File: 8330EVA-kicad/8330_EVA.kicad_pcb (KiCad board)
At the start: 2 copper layers, 70 parts, among them J1 USB_B_Micro, J2 Conn_Coaxial, J3 Conn_01x03_Male, J4 Conn_Coaxial, J5 Conn_Coaxial, J6 Conn_01x03_Male, T1 T1-1T-KK81, T2 T1-1T-KK81, U1 AMS1117-3.3, U2 FT232H, U3 AD8330, U4 AD8131, U5 AD5312, U6 REF192, Y1 12Mhz

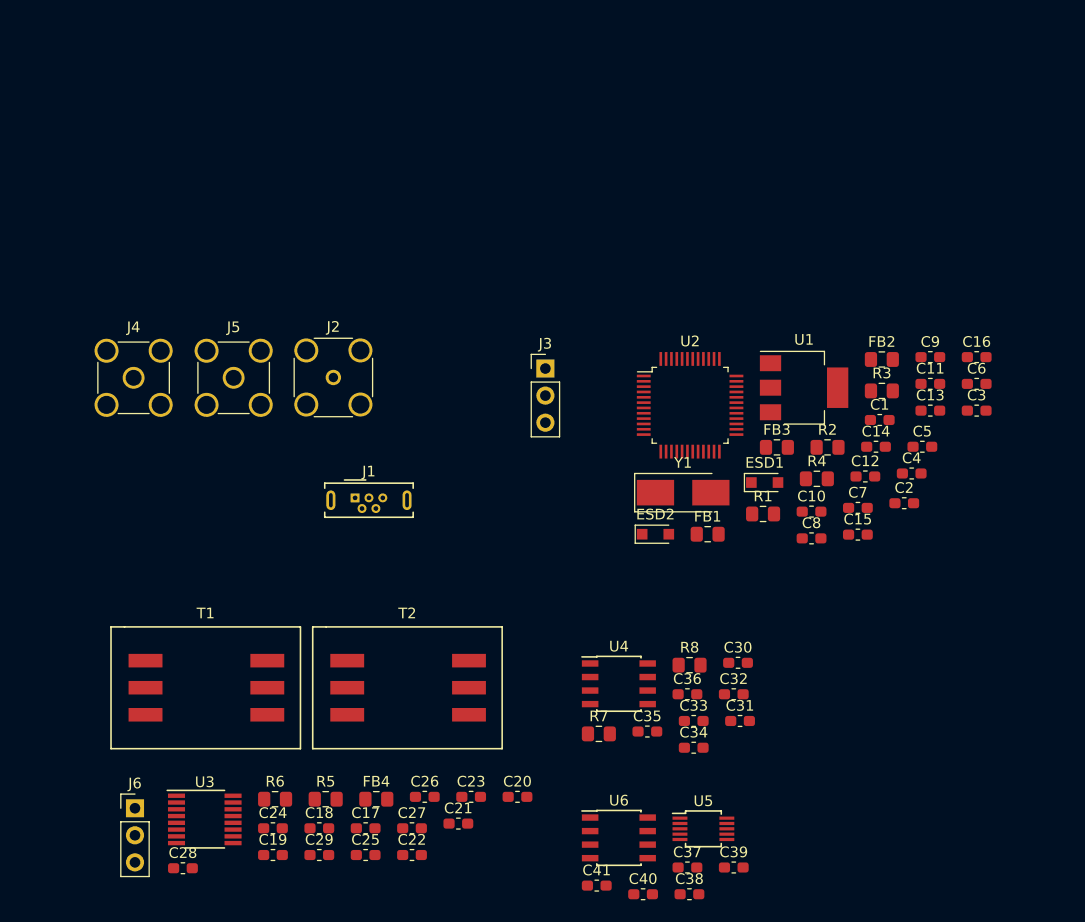
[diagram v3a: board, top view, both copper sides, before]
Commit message: Finished PCB layout, connect Earth to Ground
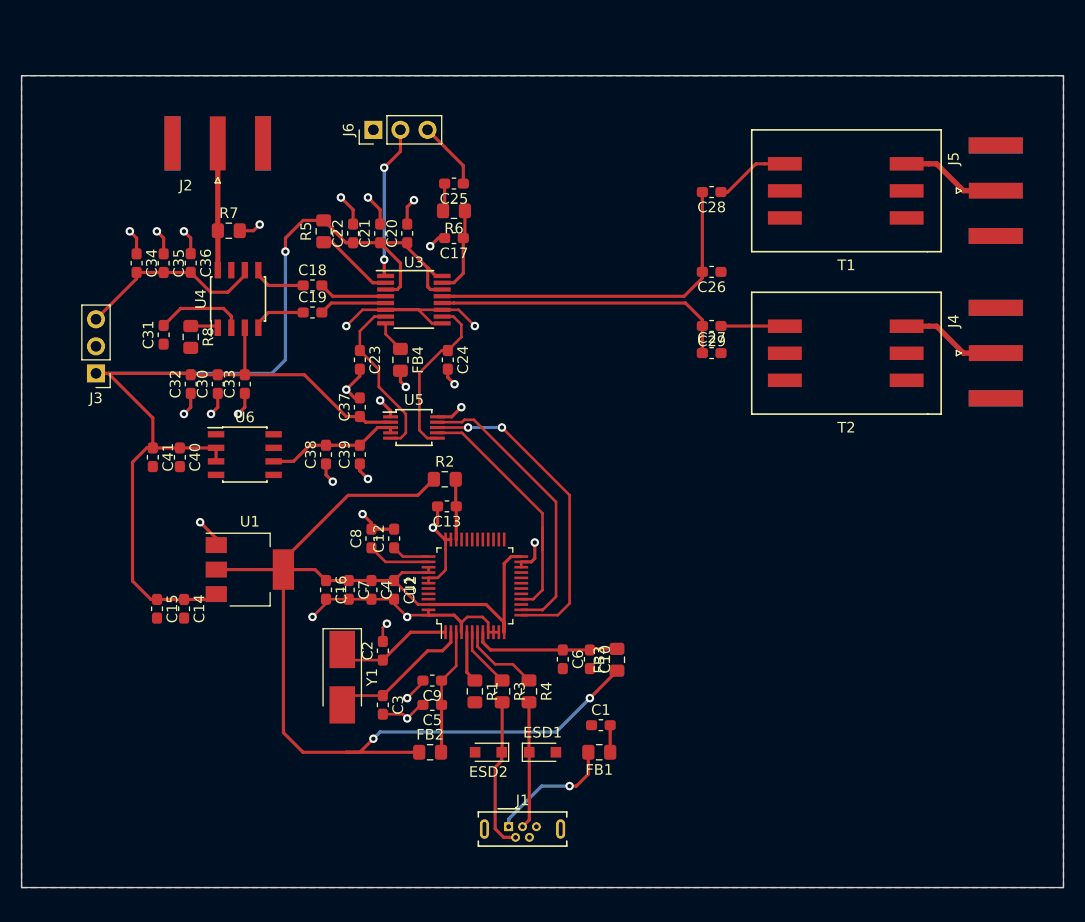
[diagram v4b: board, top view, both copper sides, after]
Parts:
- J2: footprint Connector_Coaxial:SMA_Amphenol_132134-14_Vertical -> Connector_Coaxial:SMA_Amphenol_132289_EdgeMount
- J4, J5: footprint Connector_Coaxial:SMA_Amphenol_132134-11_Vertical -> Connector_Coaxial:SMA_Amphenol_132289_EdgeMount
- moved J4 81.0 mm to (198.1, 79.4)
- moved C28 80.6 mm to (171.4, 64.3), turned to 180 degrees
- moved T1 77.0 mm to (184.2, 63.5), turned to 180 degrees
- moved J5 73.7 mm to (198.1, 64.1)
- moved C34 69.3 mm to (117.5, 70.9), turned to 270 degrees
- moved J6 67.5 mm to (139.7, 58.4), turned to 90 degrees
- moved C14 66.7 mm to (121.9, 103.4), turned to 270 degrees
- moved C15 66.1 mm to (119.4, 103.4), turned to 270 degrees
- moved C31 65.1 mm to (120.0, 77.7), turned to 90 degrees
- moved C16 64.9 mm to (135.3, 101.6), turned to 270 degrees
- moved C25 63.6 mm to (147.3, 63.5), turned to 180 degrees
- moved C35 63.2 mm to (120.0, 70.9), turned to 270 degrees
- moved C3 62.2 mm to (140.6, 112.4), turned to 270 degrees
- moved C29 61.8 mm to (171.4, 76.8), turned to 180 degrees
- moved C36 61.7 mm to (122.6, 70.9), turned to 270 degrees
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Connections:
- C1 pad 1: /USB2SPI/Ground -> Earth
- C10 pad 2: /USB2SPI/Ground -> Earth
- C11 pad 2: /USB2SPI/Ground -> Earth
- C12 pad 2: /USB2SPI/Ground -> Earth
- C13 pad 2: /USB2SPI/Ground -> Earth
- C14 pad 2: /USB2SPI/Ground -> Earth
- C15 pad 2: /USB2SPI/Ground -> Earth
- C16 pad 2: /USB2SPI/Ground -> Earth
- C2 pad 2: /USB2SPI/Ground -> Earth
- C3 pad 2: /USB2SPI/Ground -> Earth
- C4 pad 2: /USB2SPI/Ground -> Earth
- C5 pad 2: /USB2SPI/Ground -> Earth
- C6 pad 2: /USB2SPI/Ground -> Earth
- C7 pad 2: /USB2SPI/Ground -> Earth
- C8 pad 2: /USB2SPI/Ground -> Earth
- C9 pad 2: /USB2SPI/Ground -> Earth
- ESD1 pad 2: /USB2SPI/Ground -> Earth
- ESD2 pad 2: /USB2SPI/Ground -> Earth
- J1 pad 5: /USB2SPI/Ground -> Earth
- J1 pad 6: /USB2SPI/Ground -> Earth
- R1 pad 2: /USB2SPI/Ground -> Earth
- U1 pad 1: /USB2SPI/Ground -> Earth
- U2 pad 10: /USB2SPI/Ground -> Earth
- U2 pad 11: /USB2SPI/Ground -> Earth
- U2 pad 22: /USB2SPI/Ground -> Earth
- U2 pad 23: /USB2SPI/Ground -> Earth
- U2 pad 35: /USB2SPI/Ground -> Earth
- U2 pad 36: /USB2SPI/Ground -> Earth
- U2 pad 4: /USB2SPI/Ground -> Earth
- U2 pad 41: /USB2SPI/Ground -> Earth
- U2 pad 42: /USB2SPI/Ground -> Earth
- U2 pad 47: /USB2SPI/Ground -> Earth
- U2 pad 48: /USB2SPI/Ground -> Earth
- U2 pad 9: /USB2SPI/Ground -> Earth
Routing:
- net /DAC/VCC_+5V: track 0.00 -> 131.1 mm, vias 0 -> 1
- net /USB2SPI/VCCIO: track 0.00 -> 117.9 mm, vias 0 -> 2
- net Earth: track 0.00 -> 112.3 mm, vias 0 -> 29
- net Net-(C26-Pad2): track 0.00 -> 33.2 mm
- net /USB2SPI/MPSSE_SCK: track 0.00 -> 29.9 mm, vias 0 -> 2
- net Net-(C27-Pad1): track 0.00 -> 28.2 mm
- net /USB2SPI/MPSSE_MOSI: track 0.00 -> 27.1 mm
- net /USB2SPI/MPSSE_CS: track 0.00 -> 24.6 mm
- net /VCA/VEE_-5V: track 0.00 -> 18.0 mm
- net /DAC/ChannelB: track 0.00 -> 16.0 mm
- net /DAC/ChannelA: track 0.00 -> 16.0 mm
- net Net-(J6-Pad2): track 0.00 -> 14.4 mm, vias 0 -> 2
- net /USB2SPI/USB_D-: track 0.00 -> 14.4 mm
- net /USB2SPI/VPLL: track 0.00 -> 13.9 mm
- net Net-(C3-Pad1): track 0.00 -> 13.6 mm
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- added copper zone on B.Cu, net Earth
- added copper zone on F.Cu, net Earth
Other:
- board outline added: 97.8 x 76.2 mm

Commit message: 简单修改
1. 修改了差分输出处的布线，提高对称性
2. 修改了USB接口的封装。现在使用完全表面贴装的Mini USB接口
3. 在电路板上添加了要求的信息
4. 生成了BOM表和Gerber文件
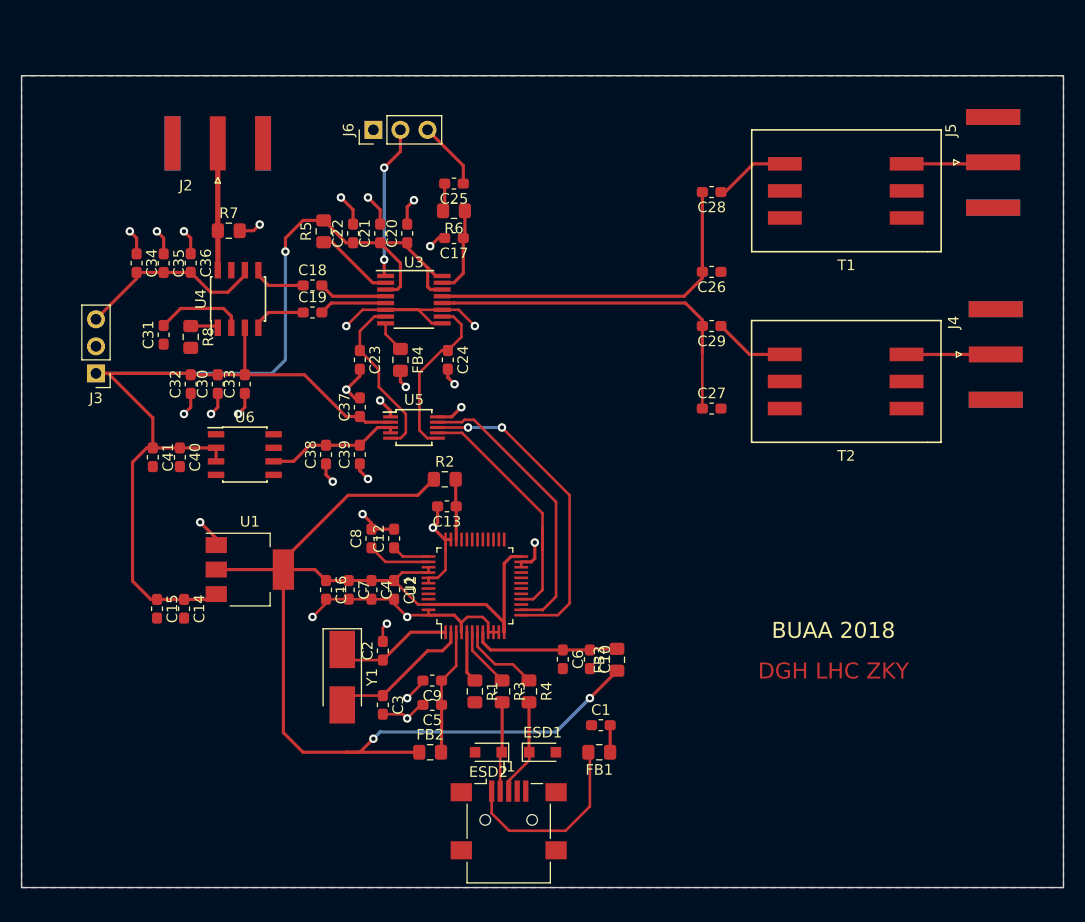
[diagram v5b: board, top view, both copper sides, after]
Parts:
- J1: footprint Connector_USB:USB_Micro-B_Wuerth_614105150721_Vertical -> Connector_USB:USB_Mini-B_Lumberg_2486_01_Horizontal
- moved C27 5.21 mm to (171.4, 84.6)
- moved J5 2.68 mm to (197.9, 61.5)
- moved T2 2.65 mm to (184.1, 81.4)
- moved J1 0.64 mm to (152.4, 123.2)
- moved J4 0.13 mm to (198.1, 79.5)
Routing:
- net /USB2SPI/VBUS: track 12.0 -> 17.7 mm, vias 1 -> 0
- net /USB2SPI/USB_D-: track 14.4 -> 8.70 mm
- net Net-(C27-Pad1): track 28.2 -> 33.4 mm
- net /USB2SPI/USB_D+: track 11.9 -> 9.79 mm
- net /VCA/OPLO: track 9.41 -> 8.13 mm
- net /VCA/OPHI: track 9.41 -> 8.34 mm
- net Net-(C29-Pad1): track 6.00 -> 6.89 mm
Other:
- board text added: "BUAA 2018"
- board text added: "DGH LHC ZKY"

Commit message: 添加M3安装孔，调整SMA焊盘位置
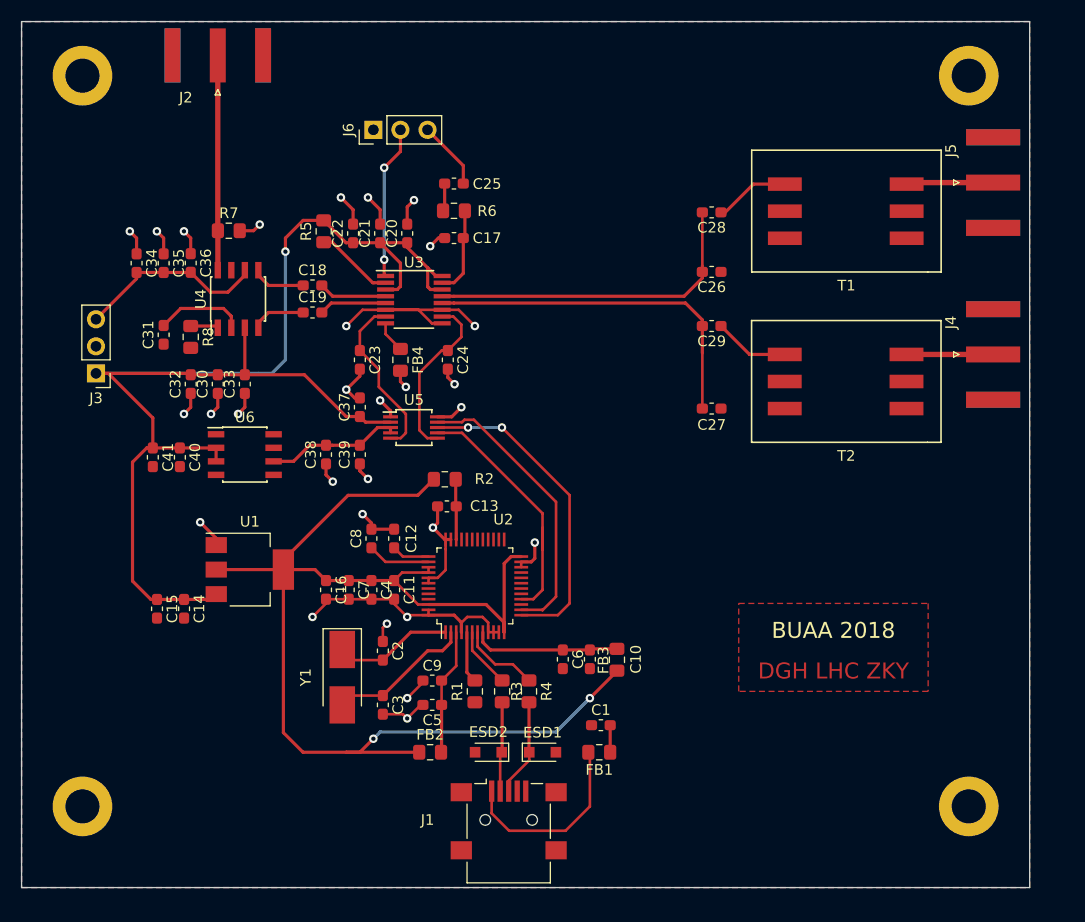
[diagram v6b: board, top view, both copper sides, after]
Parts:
- added REF**: MountingHole_3.2mm_M3_DIN965_Pad, MountingHole:MountingHole_3.2mm_M3_DIN965_Pad, F.Cu at (112.4, 53.3)
- added REF**: MountingHole_3.2mm_M3_DIN965_Pad, MountingHole:MountingHole_3.2mm_M3_DIN965_Pad, F.Cu at (112.4, 121.9)
- added REF**: MountingHole_3.2mm_M3_DIN965_Pad, MountingHole:MountingHole_3.2mm_M3_DIN965_Pad, F.Cu at (195.6, 53.3)
- added REF**: MountingHole_3.2mm_M3_DIN965_Pad, MountingHole:MountingHole_3.2mm_M3_DIN965_Pad, F.Cu at (195.6, 121.9)
- moved J2 8.25 mm to (125.1, 51.4)
- moved C28 1.91 mm to (171.4, 66.2)
- moved T1 1.91 mm to (184.2, 65.4)
- moved J5 1.90 mm to (197.9, 63.4)
- moved J4 0.25 mm to (197.9, 79.5)
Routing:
- net /VCA/SignalIN: track 11.9 -> 20.2 mm
- net Net-(C26-Pad2): track 33.2 -> 31.9 mm
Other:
- board size 97.8 x 76.2 mm -> 94.6 x 81.3 mm

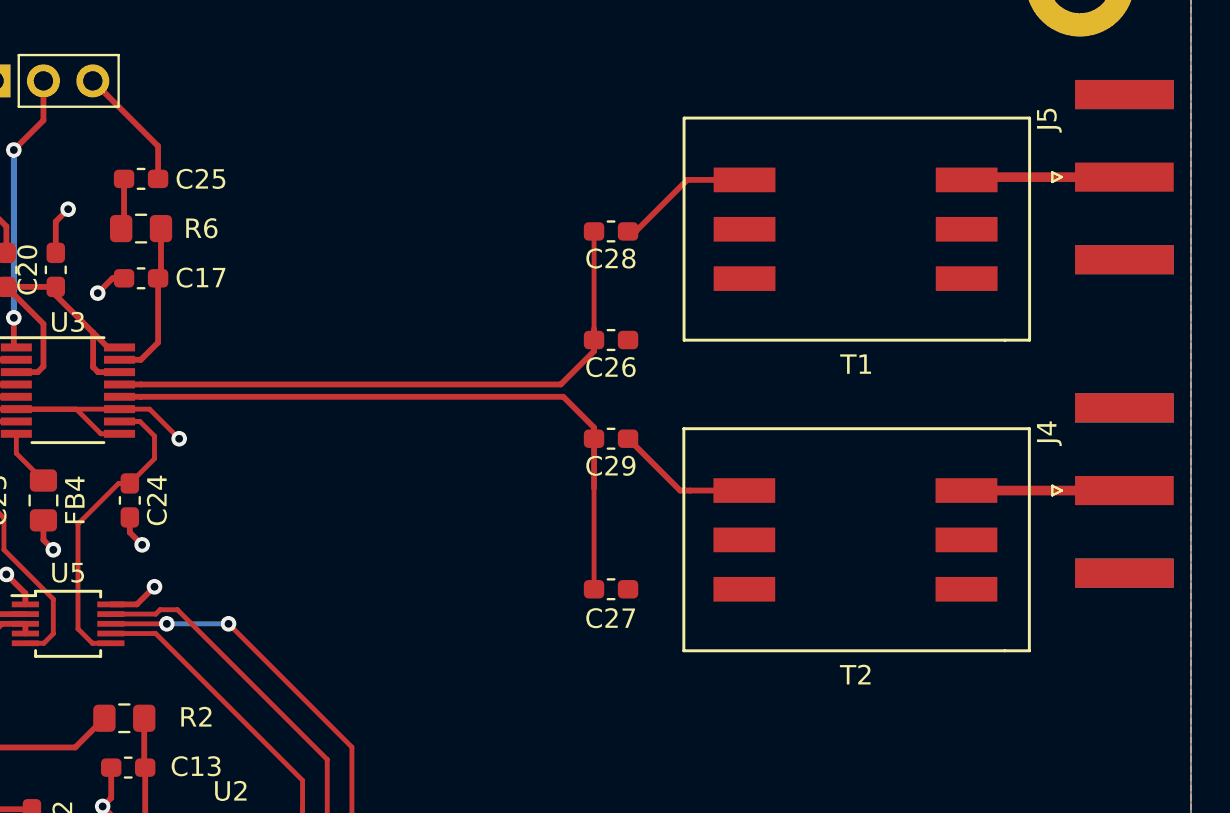
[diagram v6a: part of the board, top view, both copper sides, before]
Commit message: 改变巴伦的使用方式
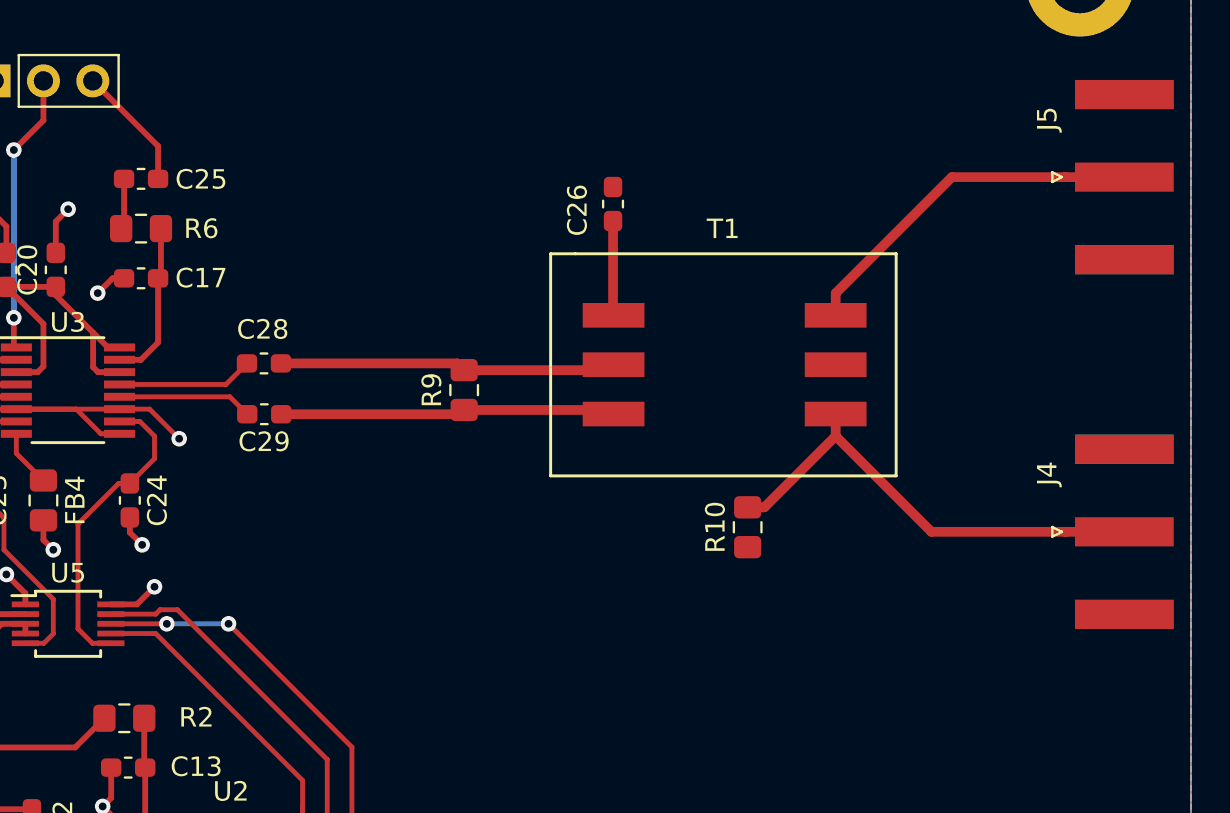
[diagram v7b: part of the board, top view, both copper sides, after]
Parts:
- removed C27: 12p, Capacitor_SMD:C_0603_1608Metric_Pad1.05x0.95mm_HandSolder
- removed T2: T1-1T-KK81, 8330EVA-footprint-extra:Mini_Circuit_RF_Transformer_SO6
- added R10: 0, Resistor_SMD:R_0805_2012Metric_Pad1.15x1.40mm_HandSolder, F.Cu at (178.5, 81.4)
- added R9: 220, Resistor_SMD:R_0805_2012Metric_Pad1.15x1.40mm_HandSolder, F.Cu at (163.9, 74.3)
- C26: value 12p -> 0.1u
- moved C28 19.1 mm to (153.6, 73.0)
- moved C29 17.9 mm to (153.6, 75.6)
- moved T1 10.8 mm to (177.2, 73.7), turned to 0 degrees
- moved C26 7.00 mm to (171.6, 64.8), turned to 90 degrees
- moved J4 2.12 mm to (197.9, 81.6)
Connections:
- C26 pad 1: Earth -> Net-(C26-Pad1)
- C26 pad 2: Net-(C26-Pad2) -> Earth
- C28 pad 2: Net-(C26-Pad2) -> Net-(C28-Pad2)
- T1 pad 1: Net-(T1-Pad1) -> Net-(C26-Pad1)
- T1 pad 2: Earth -> Net-(C28-Pad1)
- T1 pad 3: /VCA/OPHI -> Net-(C29-Pad1)
- T1 pad 4: Net-(C28-Pad1) -> /VCA/OPLO
- T1 pad 6: Earth -> /VCA/OPHI
- U3 pad 13: Net-(C26-Pad2) -> Net-(C28-Pad2)
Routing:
- net Net-(C26-Pad2): track 31.9 -> 0.00 mm
- net Net-(C29-Pad2): track 33.4 -> 6.95 mm
- net /VCA/OPLO: track 8.13 -> 24.1 mm
- net Net-(C28-Pad1): track 6.95 -> 17.4 mm
- net Net-(C29-Pad1): track 6.89 -> 17.3 mm
- net /VCA/OPHI: track 8.51 -> 18.5 mm
- net Net-(C28-Pad2): track 0.00 -> 7.01 mm
- net Net-(C26-Pad1): track 0.00 -> 4.90 mm
